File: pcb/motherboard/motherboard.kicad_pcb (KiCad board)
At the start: 4 copper layers, 99.1 x 29.2 mm, 10 parts, among them J1 BARREL_JACK, J2 USB-MINI-B, J3 HEADER-1x05, J4 HEADER-1x04, J6 HEADER-1x10, J7 HEADER-2x03, J8 HEADER-2x03

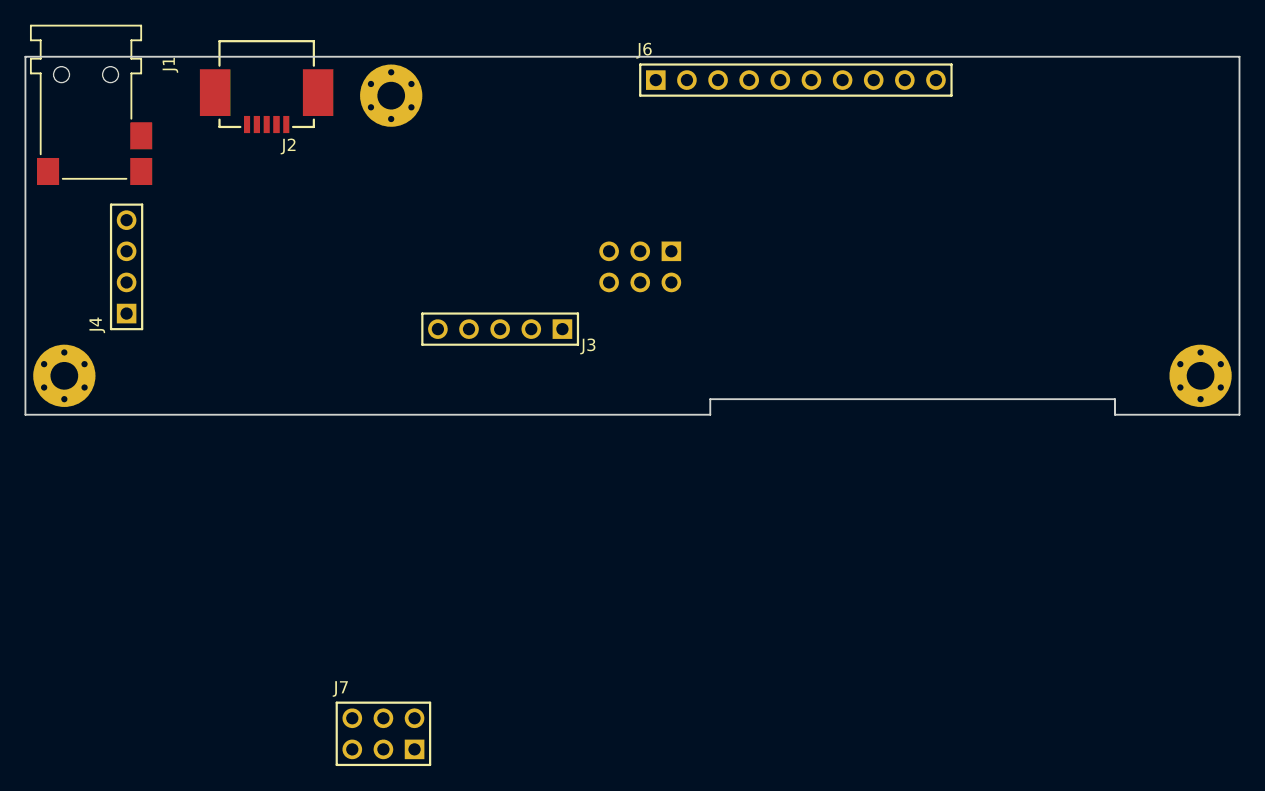
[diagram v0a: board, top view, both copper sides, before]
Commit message: Revised touch and front panel PCB, Added Motherboard PCB
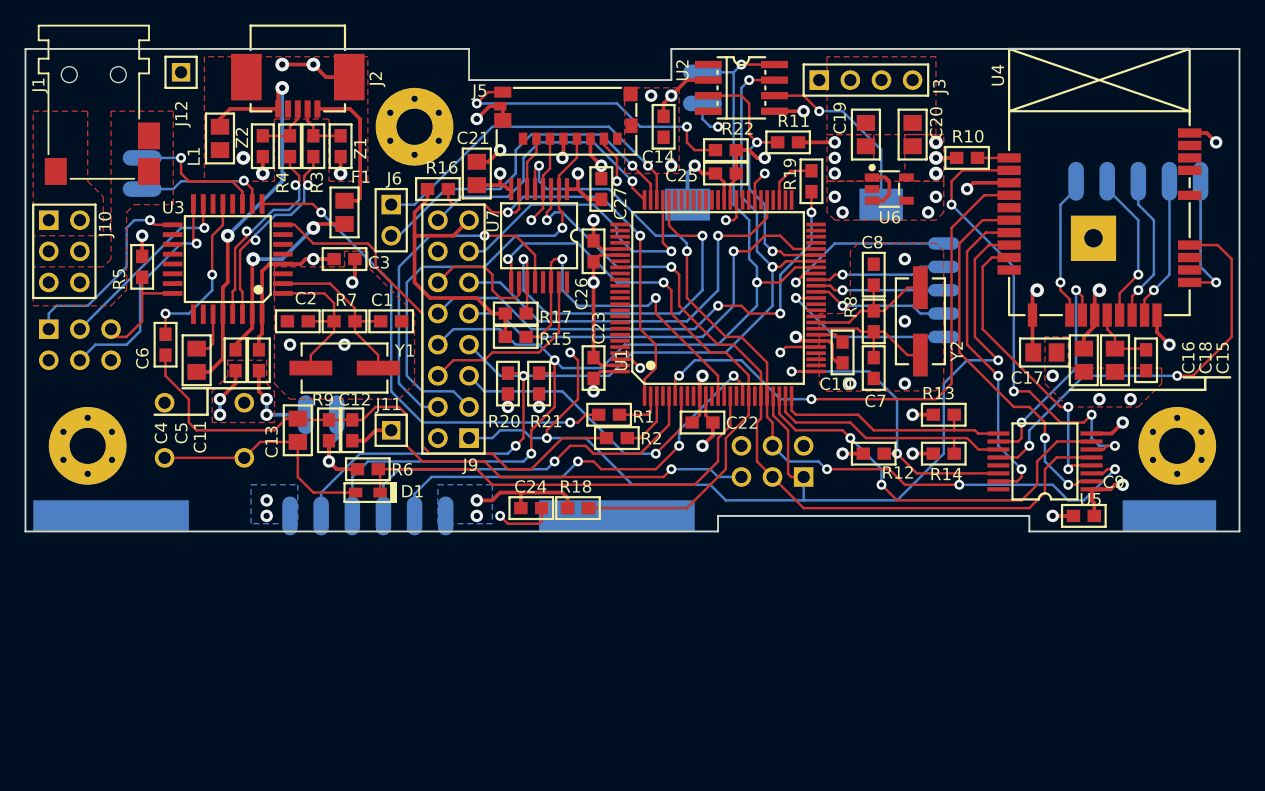
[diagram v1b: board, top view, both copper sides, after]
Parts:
- added B1: CR1220, conn-power:BC501SM, B.Cu at (169.5, 97.2)
- added C1: 20pF, smt:C-0603, F.Cu at (137.8, 106.7)
- added C10: 100nF, smt:C-0603, F.Cu at (174.6, 109.2)
- added C11: 100nF, smt:C-0603, F.Cu at (127.0, 109.9)
- added C12: 22pF, smt:C-0603, F.Cu at (134.6, 115.6)
- added C13: 1uF, smt:C-0805, F.Cu at (130.2, 115.6)
- added C14: 100nF, smt:R-0603, F.Cu at (160.0, 90.8)
- added C15: 10nF, smt:C-0603, F.Cu at (199.4, 109.9)
- added C16: 10uF, smt:C-0805, F.Cu at (194.3, 109.9)
- added C17: 10uF, smt:C-0805, F.Cu at (191.1, 109.2)
- added C18: 10uF, smt:C-0805, F.Cu at (196.8, 109.9)
- added C19: 1uF, smt:C-0805, F.Cu at (176.5, 91.4)
- added C2: 20pF, smt:C-0603, F.Cu at (130.2, 106.7)
- added C20: 1uF, smt:C-0805, F.Cu at (180.3, 91.4)
- added C21: 10uF, smt:C-0805, F.Cu at (144.8, 94.6)
- added C22: 100nF, smt:C-0603, F.Cu at (163.2, 114.9)
- added C23: 100nF, smt:C-0603, F.Cu at (154.3, 110.5)
- added C24: 100nF, smt:C-0603, F.Cu at (149.2, 121.9)
- added C25: 100nF, smt:C-0603, F.Cu at (165.1, 94.6)
- added C26: 100nF, smt:C-0603, F.Cu at (154.3, 101.0)
- added C27: 100nF, smt:C-0603, F.Cu at (154.9, 95.9)
- added C3: 100nF, smt:C-0603, F.Cu at (134.0, 101.6)
- added C4: 1uF, smt:C-0805, F.Cu at (121.9, 109.9)
- added C5: 100nF, smt:C-0603, F.Cu at (125.1, 109.9)
- added C6: 100nF, smt:C-0603, F.Cu at (119.4, 108.6)
- added C7: 20pF, smt:C-0603, F.Cu at (177.2, 110.5)
- added C8: 20pF, smt:C-0603, F.Cu at (177.2, 102.9)
- added C9: 100nF, smt:C-0603, F.Cu at (194.3, 122.6)
- added D1: DIODE, smt:SOD-323, F.Cu at (135.9, 120.7)
- added F1: 500mA, smt:FER-0805, F.Cu at (134.0, 97.8)
- added H4: HEADER-1x01, conn-wire-pads:SolderPad-100x500, B.Cu at (114.9, 122.6)
- added H5: HEADER-1x01, conn-wire-pads:SolderPad-100x500, B.Cu at (156.2, 122.6)
- added H6: HEADER-1x01, conn-wire-pads:SolderPad-100x300, B.Cu at (201.3, 122.6)
- added J10: PSU, conn-header:HDR-M-2x03, F.Cu at (111.1, 101.0)
- added J11: HEADER-1x01, conn-header:HDR-M-1x01, F.Cu at (137.8, 115.6)
- added J12: HEADER-1x01, conn-header:HDR-M-1x01, F.Cu at (120.7, 86.4)
- added J13: USB-LED, conn-wire-pads:WP-50mil-1x02, B.Cu at (117.5, 94.6)
- added J14: EXT, conn-wire-pads:WP-40mil-1x05, B.Cu at (182.9, 104.1)
- added J15: EXT-PW, conn-wire-pads:WP-50mil-1x02, B.Cu at (132.1, 114.3)
- added J16: EXT-I2C, conn-wire-pads:WP-50mil-1x02, B.Cu at (163.2, 87.6)
- added J17: WIFI-GPIO, conn-wire-pads:WP-50mil-1x05, B.Cu at (198.8, 95.2)
- added J5: Micro_SD, conn-io:MOLEX-MICROSD-475710001, F.Cu at (152.4, 87.6)
- added J9: DB I/O, conn-header:HDR-M-2x08, F.Cu at (142.9, 107.3)
- added L1: BLM21, smt:FER-0805, F.Cu at (123.8, 91.8)
- added R1: 1k, smt:R-0603, F.Cu at (155.6, 114.3)
- added R10: 100k, smt:R-0603, F.Cu at (184.8, 93.3)
- added R11: 10k, smt:R-0603, F.Cu at (170.2, 92.1)
- added R12: 100k, smt:R-0603, F.Cu at (177.2, 117.5)
- added R13: 100k, smt:R-0603, F.Cu at (182.9, 114.3)
- added R14: 100k, smt:R-0603, F.Cu at (182.9, 117.5)
- added R15: 100k, smt:R-0603, F.Cu at (148.0, 108.0)
- added R16: 100k, smt:R-0603, F.Cu at (141.6, 95.9)
- added R17: 100k, smt:R-0603, F.Cu at (148.0, 106.0)
- added R18: 100k, smt:R-0603, F.Cu at (153.0, 121.9)
- added R19: 300, smt:C-0603, F.Cu at (172.1, 95.2)
- added R2: 1k, smt:R-0603, F.Cu at (156.2, 116.2)
- added R20: 10k, smt:C-0603, F.Cu at (147.3, 111.8)
- added R21: 10k, smt:C-0603, F.Cu at (149.9, 111.8)
- added R22: 10k, smt:C-0603, F.Cu at (165.1, 92.7)
- added R3: 22, smt:R-0603, F.Cu at (131.4, 92.4)
- added R4: 22, smt:R-0603, F.Cu at (129.5, 92.4)
- added R5: 10k, smt:R-0603, F.Cu at (117.5, 102.2)
- added R6: 10k, smt:R-0603, F.Cu at (135.9, 118.7)
- added R7: 1M, smt:R-0603, F.Cu at (134.0, 106.7)
- added R8: 1M, smt:R-0603, F.Cu at (177.2, 106.7)
- added R9: 10k, smt:R-0603, F.Cu at (132.7, 115.6)
- added REF**: VAL**, symbols:SIGNATURE_SILK, B.Cu at (130.3, 103.1)
- added REF**: VAL**, symbols:LOGO-OSHW-250, B.Cu at (184.4, 115.1)
- added SW1: RESET, switches:B3F-10XX, B.Cu at (122.6, 115.6)
- added U1: ATMEGA2560-16AU, smt-qfp:QFP-14-100, F.Cu at (164.5, 104.8)
- added U2: DS3231M, smt-soic:SOIC8, F.Cu at (166.4, 87.6)
- added U3: ATMEGA8U2-AU, smt-qfp:QFP-7-32, F.Cu at (124.5, 101.6)
- added U4: ATWINC1500-MR, misc:ATWINC1500-MR, F.Cu at (195.6, 84.5)
- added U5: 74X4050, smt-sop:SSOP16, F.Cu at (191.1, 118.1)
- added U6: AP2112K-3.3, smt-sot:SOT23-5, F.Cu at (178.4, 95.9)
- added U7: 74X4050, smt-sop:SSOP16, F.Cu at (149.9, 99.7)
- added Y1: 16.00 MHz, crystals:HC49USX, F.Cu at (134.0, 110.5)
- added Y2: 16.00 MHz, crystals:HC49USX, F.Cu at (181.0, 106.7)
- added Z1: PGB1010603, smt:FER-0603, F.Cu at (133.7, 92.4)
- added Z2: PGB1010603, smt:FER-0603, F.Cu at (127.3, 92.4)
- H1, H2, H3: footprint Conn-Wire-Pads:Hole-Screw-#2 -> conn-wire-pads:Hole-Screw-#4
- J1: value BARREL_JACK -> DC_IN; footprint Conn-Power:CUI-P1J-021-SMT -> conn-power:CUI-P1J-021-SMT
- J2: footprint Conn-IO:USB-MB_UX60SC-MB-5ST -> conn-io:USB-MB_UX60SC-MB-5ST
- J3: value HEADER-1x05 -> DB PWR; footprint Conn-Header:HDR-M-1x05 -> conn-header:HDR-M-1x04
- J4: value HEADER-1x04 -> ICSP-USB; footprint Conn-Header:HDR-M-1x04 -> conn-header:HDR-M-2x03; moved to B.Cu
- J6: value HEADER-1x10 -> PSU-SIG; footprint Conn-Header:HDR-M-1x10 -> conn-header:HDR-M-1x02
- J7: value HEADER-2x03 -> ICSP; footprint Conn-Header:HDR-M-2x03 -> conn-header:HDR-M-2x03; moved to B.Cu
- J8: value HEADER-2x03 -> FRONT PANEL; footprint Conn-Header:HDR-M-2x03 -> conn-wire-pads:WP-50mil-1x06
- moved J7 38.8 mm to (168.9, 118.1), turned to 180 degrees
- moved J3 36.1 mm to (176.5, 87.0), turned to 0 degrees
- moved J6 34.9 mm to (137.8, 98.4), turned to 270 degrees
- moved J8 30.1 mm to (135.9, 122.6)
- moved J4 7.41 mm to (112.4, 108.6), turned to 0 degrees
- moved H1 6.02 mm to (113.0, 116.8)
- moved H2 6.02 mm to (201.9, 116.8)
- moved H3 3.18 mm to (139.7, 90.8)
- moved J2 2.84 mm to (130.2, 82.5)
- moved J1 0.64 mm to (113.0, 82.5)
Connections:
- J1 pad 1: /Power suply/VIN -> /VIN
- J2 pad 1: Net-(J2-Pad1) -> /USB Serial/UVCC_IN
- J2 pad 2: Net-(J2-Pad2) -> /USB Serial/D_IN-
- J2 pad 3: Net-(J2-Pad3) -> /USB Serial/D_IN+
- J2 pad 5: Net-(J2-Pad5) -> /USB Serial/UGND
- J2 pad SH: Net-(J2-PadSH) -> /USB Serial/USHLD
- J3 pad 1: Net-(J3-Pad1) -> +5V
- J3 pad 2: Net-(J3-Pad2) -> +5V
- J3 pad 3: Net-(J3-Pad3) -> GND
- J3 pad 4: Net-(J3-Pad4) -> GND
- J4 pad 1: Net-(J4-Pad1) -> /USB Serial/MISO-USB
- J4 pad 2: Net-(J4-Pad2) -> +5V
- J4 pad 3: Net-(J4-Pad3) -> /USB Serial/SCK-USB
- J4 pad 4: Net-(J4-Pad4) -> /USB Serial/MOSI-USB
- J6 pad 1: Net-(J6-Pad1) -> /LOW_BATT
- J6 pad 2: Net-(J6-Pad2) -> /ON_BATT
- J7 pad 1: Net-(J7-Pad1) -> /MISO
- J7 pad 2: Net-(J7-Pad2) -> +5V
- J7 pad 3: Net-(J7-Pad3) -> /SCK
- J7 pad 4: Net-(J7-Pad4) -> /MOSI
- J7 pad 5: Net-(J7-Pad5) -> /RESET
- J7 pad 6: Net-(J7-Pad6) -> GND
- J8 pad 1: Net-(J8-Pad1) -> +5V
- J8 pad 2: Net-(J8-Pad2) -> /SDA
- J8 pad 3: Net-(J8-Pad3) -> /SCL
- J8 pad 4: Net-(J8-Pad4) -> /OLRST
- J8 pad 5: Net-(J8-Pad5) -> /ALS_INT
- J8 pad 6: Net-(J8-Pad6) -> GND
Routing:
- net /MISO: track 0.00 -> 104.8 mm, vias 0 -> 4
- net /SCL: track 0.00 -> 89.5 mm, vias 0 -> 4
- net /SDA: track 0.00 -> 88.1 mm, vias 0 -> 5
- net GND: track 0.00 -> 83.9 mm, vias 0 -> 36
- net /RESET: track 0.00 -> 71.5 mm, vias 0 -> 2
- net /MOSI: track 0.00 -> 70.5 mm, vias 0 -> 5
- net /SCK: track 0.00 -> 66.4 mm, vias 0 -> 2
- net +5V: track 0.00 -> 63.2 mm, vias 0 -> 17
- net DVDD: track 0.00 -> 49.5 mm, vias 0 -> 3
- net /CRST: track 0.00 -> 48.7 mm, vias 0 -> 2
- net /WIRQ: track 0.00 -> 44.9 mm, vias 0 -> 2
- net Net-(R2-Pad1): track 0.00 -> 42.8 mm
- net /PIX_CLK: track 0.00 -> 41.6 mm, vias 0 -> 3
- net Net-(R1-Pad1): track 0.00 -> 40.3 mm, vias 0 -> 2
- net /PIX_SHDN: track 0.00 -> 39.3 mm, vias 0 -> 1
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- added copper zone on F.Cu, net +3V3
- added copper zone on Power, net +3V3
- added copper zone on B.Cu, net +5V
- added copper zone on F.Cu, net +5V
- added copper zone on Power, net +5V
- added copper zone on F.Cu, net /USB Serial/USHLD
- added copper zone on GND, net /USB Serial/USHLD
- added copper zone on F.Cu, net /VIN
- added copper zone on B.Cu, net GND
- added copper zone on F.Cu, net GND
- added copper zone on GND, net GND
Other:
- board size 99.1 x 29.2 mm -> 99.1 x 39.4 mm
- net class Default: clearance 0.254 -> 0.2032; trace_width 0.254 -> 0.2032; via_dia 1.0668 -> 0.8128; via_drill 0.5588 -> 0.4064
- net class Power: clearance 0.4064 -> 0.2032; via_dia 1.3716 -> 1.016; via_drill 0.6096 -> 0.508
- rule trace_clearance: 0.254 -> 0.2032
- board text added: "+"
- board text added: "+5V"
- board text added: "Alarm Clock V3"
- board text added: "CR-1220"
- board text added: "GND"
- board text added: "GPIO_1"
- board text added: "GPIO_3"
- board text added: "L-ERR"
- board text added: "L-NET"
- board text added: "L-RXD"
- board text added: "L-TXD"
- board text added: "L-WIFI"
- board text added: "P42"
- board text added: "P43"
- board text added: "P44"
- board text added: "P45"
- board text added: "P46"
- board text added: "PC-05"
- board text added: "REV. A"
- board text added: "SCL"
- board text added: "SDA"
- board text added: "www.bfrigon.com"

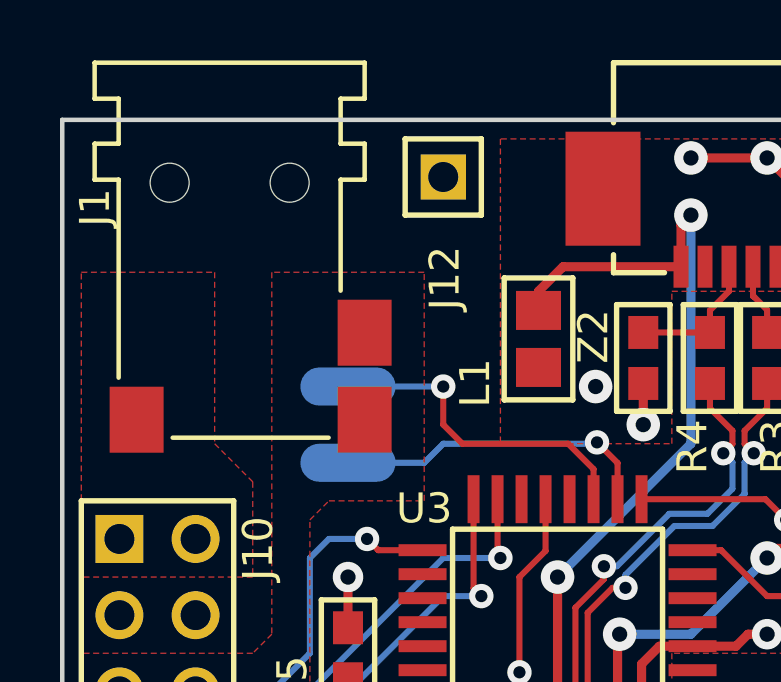
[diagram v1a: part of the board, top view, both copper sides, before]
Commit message: Changed DC jack position on motherboard
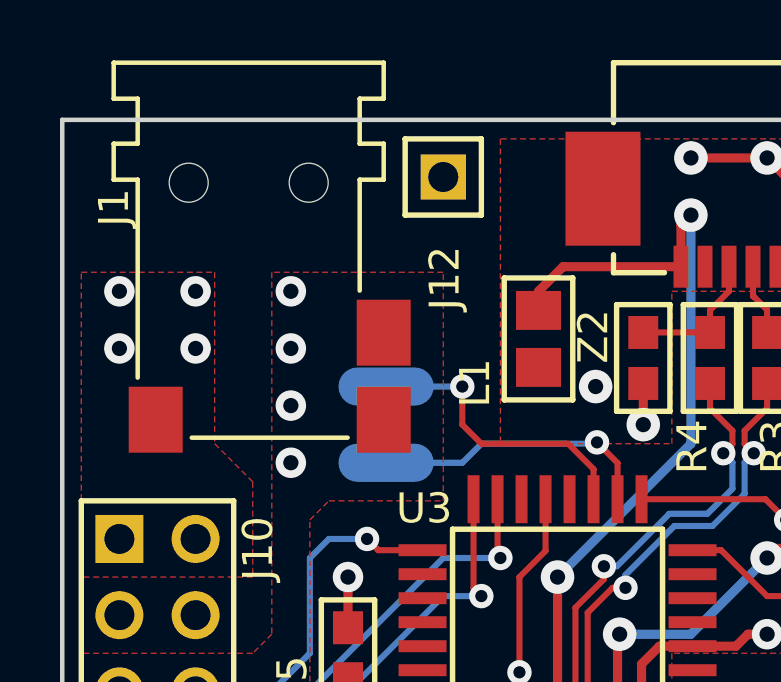
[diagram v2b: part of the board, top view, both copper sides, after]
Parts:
- moved J13 1.27 mm to (118.7, 94.6)
- moved J1 0.64 mm to (113.7, 82.5)
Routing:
- net /USB Serial/LED_TX: track 11.1 -> 9.80 mm
- net /USB Serial/LED_RX: track 10.8 -> 9.49 mm
- net GND: vias 36 -> 40
- net /VIN: vias 0 -> 4
- added copper zone on Power, net /VIN
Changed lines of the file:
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@@
     (thickness 1.6)
     (drawings 66)
-    (tracks 1120)
+    (tracks 1128)
     (zones 0)
     (modules 90)
@@
     (last_trace_width 0.2032)
     (trace_clearance 0.2032)
-    (zone_clearance 0.508)
+    (zone_clearance 0.4064)
     (zone_45_only yes)
     (trace_min 0.2)
@@
     (mod_text_size 1 1)
     (mod_text_width 0.15)
-    (pad_size 7.62 1.905)
-    (pad_drill 0)
+    (pad_size 1.6 1.6)
+    (pad_drill 1)
     (pad_to_mask_clearance 0.2)
     (aux_axis_origin 107.95 123.825)
@@
   )
   (module conn-power:CUI-P1J-021-SMT (layer F.Cu)
-    (at 113.03 82.55 270)
+    (at 113.665 82.55 270)
     (descr "Power Jack - 1.65mm ID 5.5mm OD")
     (tags "dc jack")
@@
   )
   (module conn-wire-pads:WP-50mil-1x02 (layer B.Cu)
-    (at 117.475 94.615 270)
+    (at 118.745 94.615 270)
     (descr "Wire pads - 50mil x 125mil - Single row, 2 pos.")
     (attr virtual)
@@
   (via (at 191.77 122.555) (size 1.016) (drill 0.508) (layers F.Cu B.Cu) (net 1))
   (segment (start 191.77 122.555) (end 193.46 122.555) (width 0.3048) (layer F.Cu) (net 1))
+  (via (at 115.57 90.17) (size 1.016) (drill 0.508) (layers F.Cu B.Cu) (net 1))
+  (via (at 115.57 92.075) (size 1.016) (drill 0.508) (layers F.Cu B.Cu) (net 1))
+  (via (at 115.57 93.98) (size 1.016) (drill 0.508) (layers F.Cu B.Cu) (net 1))
+  (via (at 115.57 95.885) (size 1.016) (drill 0.508) (layers F.Cu B.Cu) (net 1))
   (segment (start 170.4468 119.38) (end 171.45 119.38) (width 0.2032) (layer F.Cu) (net 54) (status 20))
   (segment (start 170.18 119.1132) (end 170.4468 119.38) (width 0.2032) (layer F.Cu) (net 54))
@@
   (segment (start 152.4 114.935) (end 153.035 114.935) (width 0.2032) (layer F.Cu) (net 74))
   (segment (start 153.035 114.935) (end 153.67 114.3) (width 0.2032) (layer F.Cu) (net 74))
+  (via (at 112.395 90.17) (size 1.016) (drill 0.508) (layers F.Cu B.Cu) (net 85))
+  (via (at 112.395 92.075) (size 1.016) (drill 0.508) (layers F.Cu B.Cu) (net 85))
+  (via (at 109.855 90.17) (size 1.016) (drill 0.508) (layers F.Cu B.Cu) (net 85))
+  (via (at 109.855 92.075) (size 1.016) (drill 0.508) (layers F.Cu B.Cu) (net 85))
   (segment (start 128.96 104.4) (end 132.34 104.4) (width 0.2032) (layer F.Cu) (net 86) (status 10))
   (segment (start 132.34 104.4) (end 133.135 105.195) (width 0.2032) (layer F.Cu) (net 86))
@@
   (segment (start 196.85 108.905) (end 199.29 108.905) (width 0.2032) (layer F.Cu) (net 164) (status 30))
   (segment (start 188.214 93.345) (end 185.635 93.345) (width 0.2032) (layer F.Cu) (net 165) (status 30))
-  (segment (start 125.66 97.1) (end 125.66 96.0968) (width 0.2032) (layer F.Cu) (net 166) (status 1000010))
-  (segment (start 125.66 96.0968) (end 124.8132 95.25) (width 0.2032) (layer F.Cu) (net 166) (status 1000000))
-  (segment (start 124.8132 95.25) (end 121.285 95.25) (width 0.2032) (layer F.Cu) (net 166) (status 1000000))
-  (segment (start 121.285 95.25) (end 120.65 94.615) (width 0.2032) (layer F.Cu) (net 166) (status 1000000))
-  (segment (start 120.65 94.615) (end 120.65 93.345) (width 0.2032) (layer F.Cu) (net 166) (status 1000000))
-  (segment (start 120.65 93.345) (end 117.475 93.345) (width 0.2032) (layer B.Cu) (net 166) (status 1000020))
-  (via (at 120.65 93.345) (size 0.8128) (drill 0.4064) (layers F.Cu B.Cu) (net 166) (status 1000000))
+  (via (at 121.285 93.345) (size 0.8128) (drill 0.4064) (layers F.Cu B.Cu) (net 166))
+  (segment (start 124.8132 95.25) (end 125.66 96.0968) (width 0.2032) (layer F.Cu) (net 166))
+  (segment (start 121.92 95.25) (end 124.8132 95.25) (width 0.2032) (layer F.Cu) (net 166))
+  (segment (start 121.285 93.345) (end 121.285 94.615) (width 0.2032) (layer F.Cu) (net 166))
+  (segment (start 125.66 96.0968) (end 125.66 97.1) (width 0.2032) (layer F.Cu) (net 166))
+  (segment (start 121.285 94.615) (end 121.92 95.25) (width 0.2032) (layer F.Cu) (net 166))
+  (segment (start 118.745 93.345) (end 121.285 93.345) (width 0.2032) (layer B.Cu) (net 166))
   (via (at 125.774495 95.205505) (size 0.8128) (drill 0.4064) (layers F.Cu B.Cu) (net 167))
   (segment (start 126.46 95.89101) (end 125.774495 95.205505) (width 0.2032) (layer F.Cu) (net 167))
   (segment (start 126.46 97.1) (end 126.46 95.89101) (width 0.2032) (layer F.Cu) (net 167) (status 10))
-  (segment (start 120.015 95.885) (end 117.475 95.885) (width 0.2032) (layer B.Cu) (net 167) (status 20))
-  (segment (start 120.65 95.25) (end 120.015 95.885) (width 0.2032) (layer B.Cu) (net 167))
+  (segment (start 121.92 95.25) (end 121.285 95.885) (width 0.2032) (layer B.Cu) (net 167))
   (segment (start 125.774495 95.205505) (end 125.73 95.25) (width 0.2032) (layer B.Cu) (net 167))
-  (segment (start 125.73 95.25) (end 120.65 95.25) (width 0.2032) (layer B.Cu) (net 167))
+  (segment (start 125.73 95.25) (end 121.92 95.25) (width 0.2032) (layer B.Cu) (net 167))
+  (segment (start 121.285 95.885) (end 118.745 95.885) (width 0.2032) (layer B.Cu) (net 167))
   (zone (net 85) (net_name /VIN) (layer F.Cu) (hatch edge 0.508)
     (connect_pads (clearance 0.4064))
@@
     (polygon
       (pts
-        (xy 108.585 85.09) (xy 108.585 123.19) (xy 163.83 123.19) (xy 163.83 121.92) (xy 190.5 121.92)
-        (xy 190.5 123.19) (xy 206.375 123.19) (xy 206.375 91.44) (xy 181.61 91.44) (xy 181.61 85.09)
-        (xy 161.29 85.09) (xy 161.29 87.63) (xy 143.51 87.63) (xy 143.51 85.09) (xy 136.525 85.09)
-        (xy 136.525 95.885) (xy 121.92 95.885) (xy 121.92 85.09)
+        (xy 114.935 85.09) (xy 114.935 101.6) (xy 114.3 102.235) (xy 108.585 102.235) (xy 108.585 123.19)
+        (xy 163.83 123.19) (xy 163.83 121.92) (xy 190.5 121.92) (xy 190.5 123.19) (xy 206.375 123.19)
+        (xy 206.375 91.44) (xy 181.61 91.44) (xy 181.61 85.09) (xy 161.29 85.09) (xy 161.29 87.63)
+        (xy 143.51 87.63) (xy 143.51 85.09) (xy 136.525 85.09) (xy 136.525 95.885) (xy 121.92 95.885)
+        (xy 121.92 85.09)
       )
     )
@@
     (polygon
       (pts
-        (xy 120.015 89.535) (xy 114.935 89.535) (xy 114.935 101.6) (xy 114.3 102.235) (xy 108.585 102.235)
+        (xy 120.65 89.535) (xy 114.935 89.535) (xy 114.935 101.6) (xy 114.3 102.235) (xy 108.585 102.235)
         (xy 108.585 105.41) (xy 114.935 105.41) (xy 116.205 104.14) (xy 116.205 97.79) (xy 116.84 97.155)
-        (xy 120.015 97.155)
+        (xy 120.65 97.155)
       )
     )
@@
     (polygon
       (pts
-        (xy 108.585 97.155) (xy 119.38 97.155) (xy 119.38 93.98) (xy 135.255 93.98) (xy 135.255 97.155)
-        (xy 158.115 97.155) (xy 158.115 87.63) (xy 161.29 87.63) (xy 161.29 85.09) (xy 181.61 85.09)
-        (xy 181.61 90.17) (xy 177.8 90.17) (xy 177.8 121.92) (xy 163.83 121.92) (xy 163.83 123.19)
-        (xy 108.585 123.19)
+        (xy 108.585 99.695) (xy 114.935 99.695) (xy 114.935 95.885) (xy 158.115 95.885) (xy 158.115 87.63)
+        (xy 161.29 87.63) (xy 161.29 85.09) (xy 181.61 85.09) (xy 181.61 90.17) (xy 177.8 90.17)
+        (xy 177.8 121.92) (xy 163.83 121.92) (xy 163.83 123.19) (xy 108.585 123.19)
       )
     )
@@
       )
     )
+  )
+  (zone (net 85) (net_name /VIN) (layer Power) (hatch edge 0.508)
+    (priority 1)
+    (connect_pads (clearance 0.4064))
+    (min_thickness 0.254)
+    (fill yes (arc_segments 16) (thermal_gap 0.3048) (thermal_bridge_width 0.762))
+    (polygon
+      (pts
+        (xy 108.585 89.535) (xy 113.03 89.535) (xy 113.03 95.25) (xy 114.3 96.52) (xy 114.3 99.06)
+        (xy 108.585 99.06)
+      )
+    )
